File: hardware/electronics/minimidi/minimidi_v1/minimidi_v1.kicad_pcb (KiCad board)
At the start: 2 copper layers, 22 parts, among them J1 Conn_01x02_Pin, J1-I1 SJ-3524-SMT, J11-O1 SJ-3524-SMT, J2 Conn_01x02_Pin, U1 H11L1

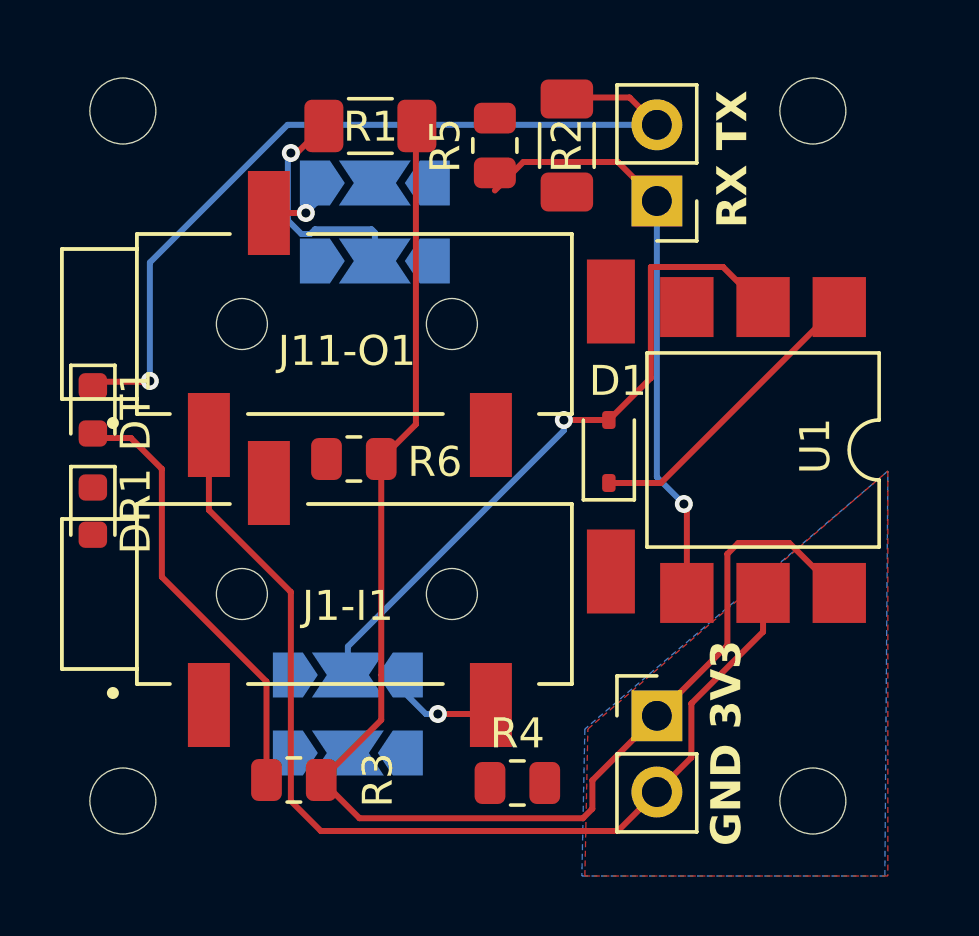
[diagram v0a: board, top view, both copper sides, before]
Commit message: Rework schemas with JLCPCB references
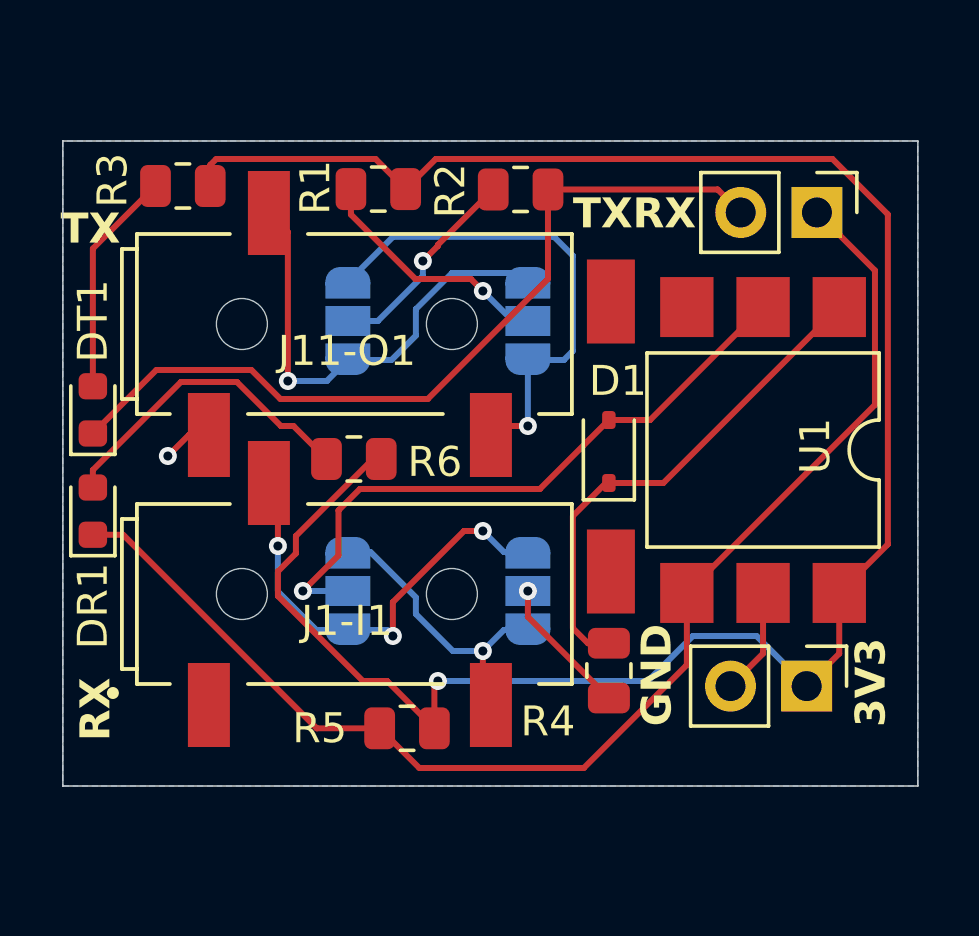
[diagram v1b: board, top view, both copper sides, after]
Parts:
- removed REF** (x4): MountingHole_2.2mm_M2, MountingHole:MountingHole_2.2mm_M2
- J1-I1, J11-O1: footprint MIDI_projects:CUI_SJ-3524-SMT -> Library:CUI_SJ-3524-SMT
- JP1, JP2, JP3, JP4: footprint Jumper:SolderJumper-3_P2.0mm_Open_TrianglePad1.0x1.5mm_NumberLabels -> Jumper:SolderJumper-3_P1.3mm_Open_RoundedPad1.0x1.5mm_NumberLabels
- R1, R2: footprint Resistor_SMD:R_1206_3216Metric_Pad1.30x1.75mm_HandSolder -> Resistor_SMD:R_0805_2012Metric
- moved R3 20.1 mm to (124.5, 85.0)
- moved R5 19.6 mm to (132.0, 103.1), turned to 0 degrees
- moved JP1 8.07 mm to (136.0, 98.5), turned to -90 degrees
- moved JP3 5.48 mm to (136.0, 89.5), turned to -90 degrees
- moved J2 5.35 mm to (145.6, 85.9), turned to -90 degrees
- moved J1 5.09 mm to (145.3, 101.7), turned to -90 degrees
- moved R4 4.83 mm to (138.7, 101.2), turned to 90 degrees
- moved JP4 4.69 mm to (130.0, 89.5), turned to -90 degrees
- moved JP2 2.80 mm to (130.0, 98.5), turned to -90 degrees
- moved R2 2.13 mm to (135.8, 85.1), turned to 180 degrees
- moved R1 2.12 mm to (131.0, 85.1)
- turned DR1 to 90 degrees
- turned DT1 to 90 degrees
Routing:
- net GND: track 34.6 -> 5.21 mm, vias 0 -> 1
- net /MIDI input 1/RX: track 19.8 -> 42.9 mm, vias 1 -> 0
- net +3V3: track 47.7 -> 70.0 mm, vias 0 -> 1
- net Net-(JP3-B): track 0.00 -> 16.3 mm, vias 0 -> 1
- net Net-(JP1-A): track 0.00 -> 14.7 mm, vias 0 -> 3
- net Net-(JP3-A): track 2.65 -> 15.6 mm
- net Net-(DR1-A): track 0.00 -> 10.6 mm
- net Net-(D1-K): track 10.0 -> 17.2 mm
- net Net-(DT1-A): track 14.5 -> 7.54 mm
- net Net-(JP4-C): track 0.00 -> 6.98 mm, vias 0 -> 1
- net Net-(JP1-B): track 3.71 -> 9.51 mm
- net Net-(JP1-C): track 0.00 -> 4.69 mm, vias 0 -> 1
- net Net-(D1-A): track 23.0 -> 21.6 mm
- net /Midi Output 1/TX: track 28.0 -> 27.8 mm, vias 1 -> 0
- removed copper zone on F.Cu, net GND
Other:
- board outline added: 28.5 x 21.5 mm
- board text added: "3V3"
- board text added: "GND"
- board text added: "RX"
- board text added: "TX"
- board text added: "TXRX"
- board text added: "Type A: 1-2 Type B: 2-3"
- board text added: "Use the same setting on all jumpers"
- board text removed: "GND 3V3"
- board text removed: "RX TX"
- board text removed: "Use the same setting on both jumpers of a port or you will be unhappy Type A: 1-2 Type B: 2-3"
